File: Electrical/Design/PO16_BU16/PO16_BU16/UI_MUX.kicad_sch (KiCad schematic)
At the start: 18 parts, among them U1 74HC4051

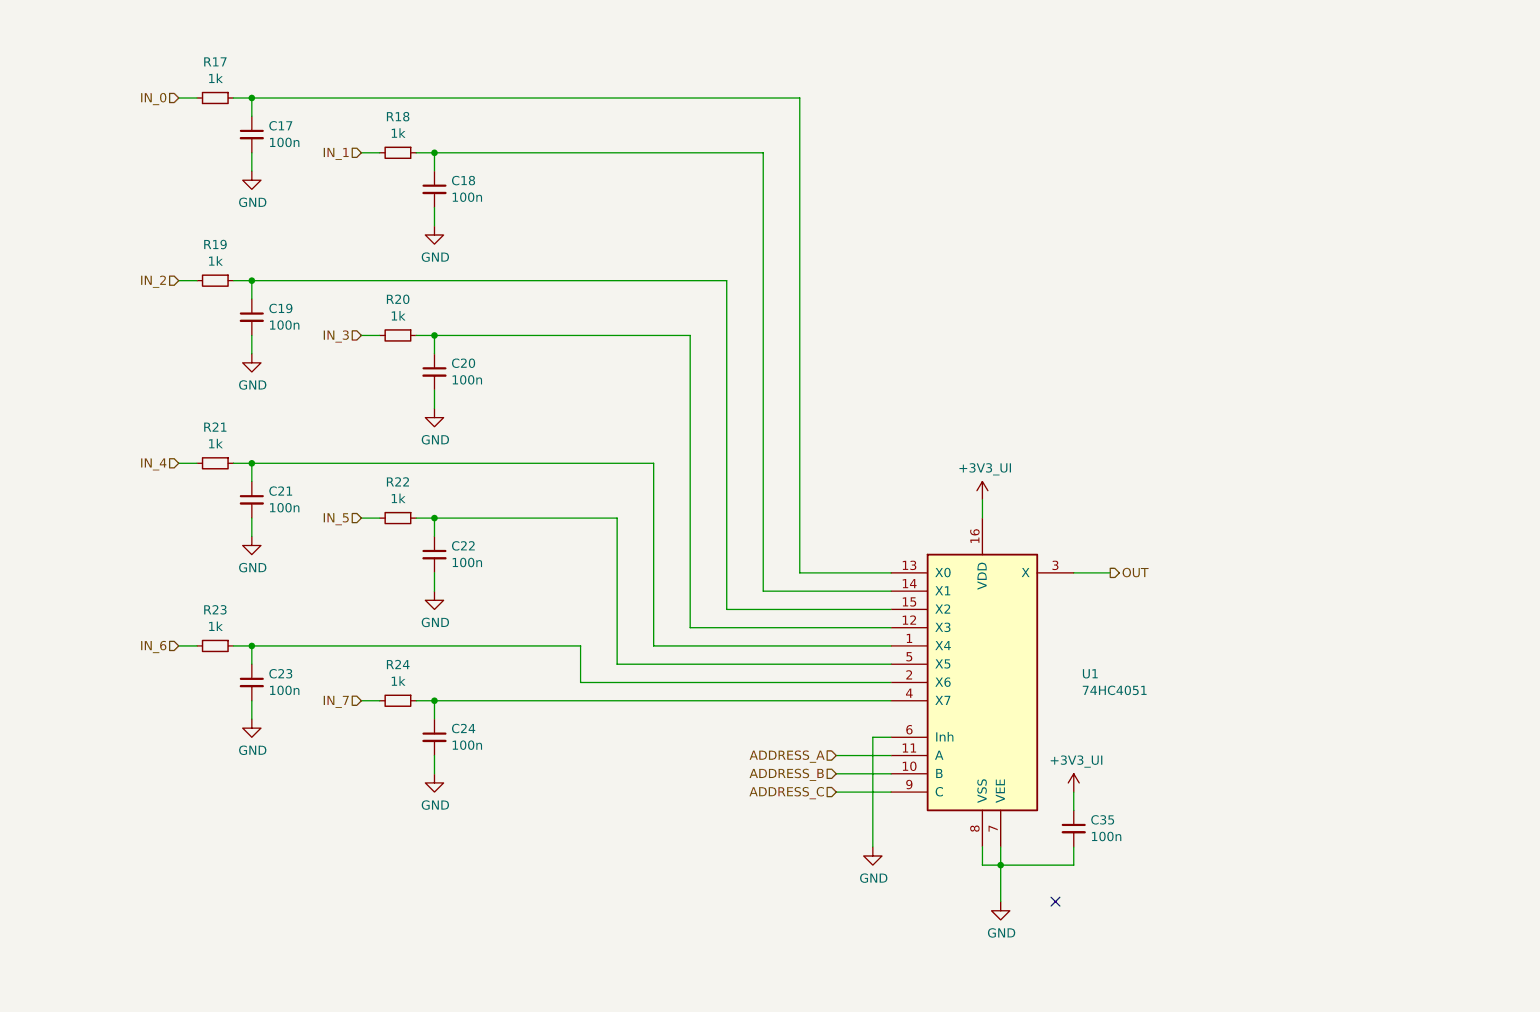
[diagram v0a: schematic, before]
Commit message: SUKU po16_bu16 cloned from pbf4
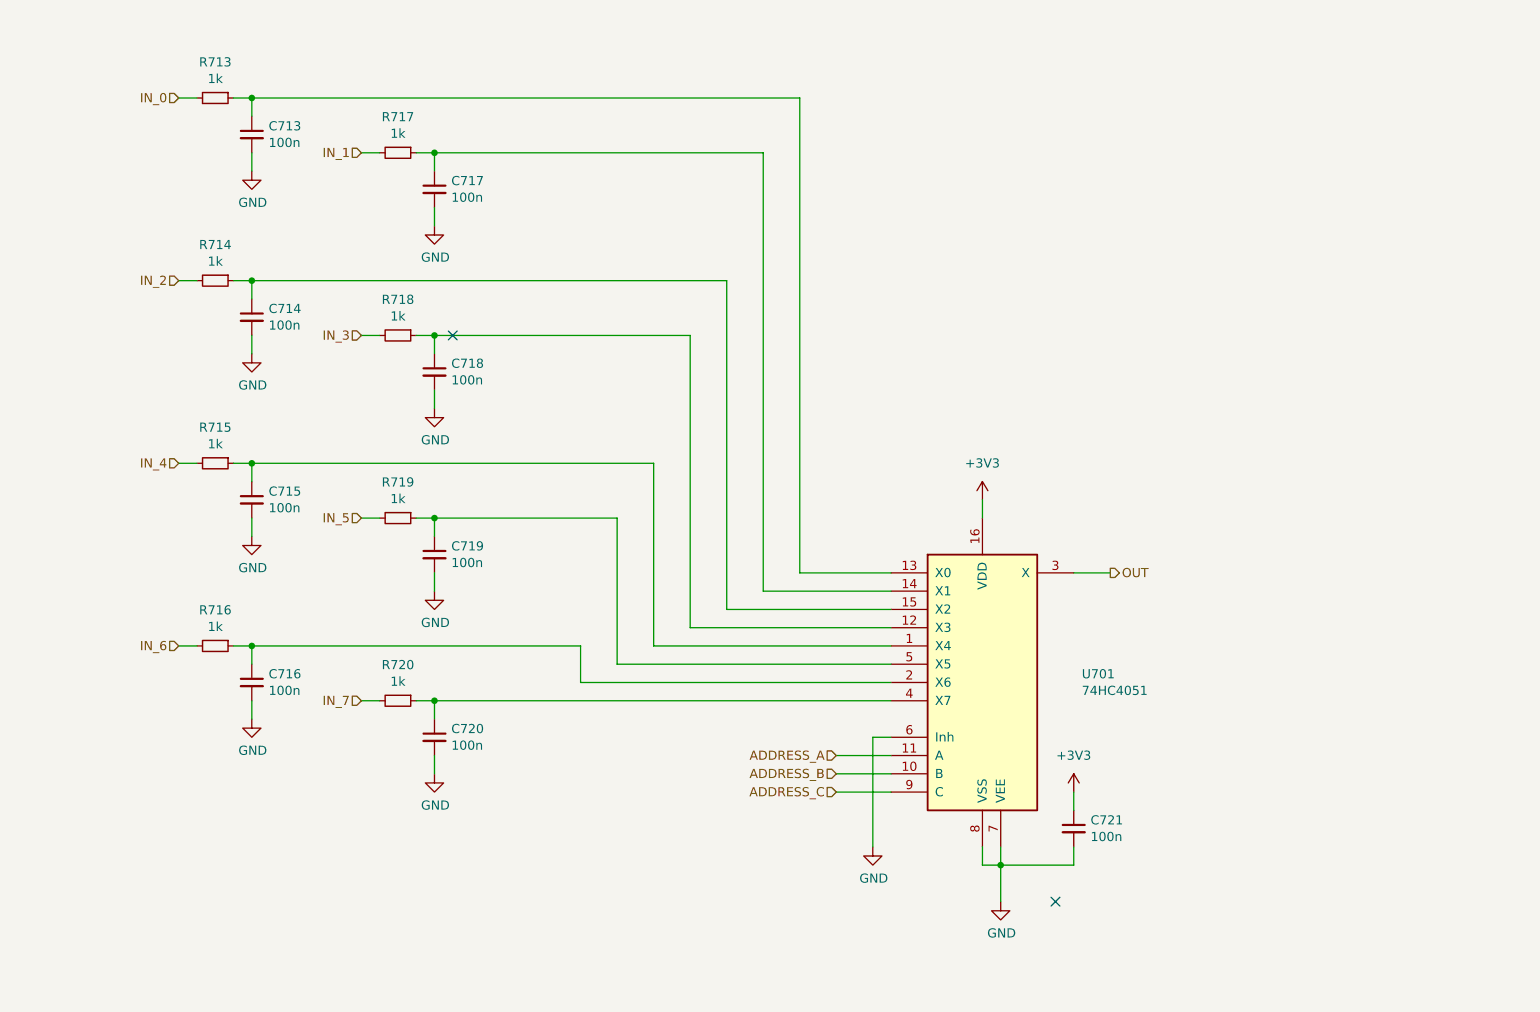
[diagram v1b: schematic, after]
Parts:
- C713: renamed from C17; footprint suku_basics:CAP_0805 -> suku_basics:CAP_0402
- C714: renamed from C19; footprint suku_basics:CAP_0805 -> suku_basics:CAP_0402
- C715: renamed from C21; footprint suku_basics:CAP_0805 -> suku_basics:CAP_0402
- C716: renamed from C23; footprint suku_basics:CAP_0805 -> suku_basics:CAP_0402
- C717: renamed from C18; footprint suku_basics:CAP_0805 -> suku_basics:CAP_0402
- C718: renamed from C20; footprint suku_basics:CAP_0805 -> suku_basics:CAP_0402
- C719: renamed from C22; footprint suku_basics:CAP_0805 -> suku_basics:CAP_0402
- C720: renamed from C24; footprint suku_basics:CAP_0805 -> suku_basics:CAP_0402
- C721: renamed from C35; footprint suku_basics:CAP_0805 -> suku_basics:CAP_0402
- R713: renamed from R17; footprint suku_basics:RES_0805 -> suku_basics:RES_0402
- R714: renamed from R19; footprint suku_basics:RES_0805 -> suku_basics:RES_0402
- R715: renamed from R21; footprint suku_basics:RES_0805 -> suku_basics:RES_0402
- R716: renamed from R23; footprint suku_basics:RES_0805 -> suku_basics:RES_0402
- R717: renamed from R18; footprint suku_basics:RES_0805 -> suku_basics:RES_0402
- R718: renamed from R20; footprint suku_basics:RES_0805 -> suku_basics:RES_0402
- R719: renamed from R22; footprint suku_basics:RES_0805 -> suku_basics:RES_0402
- R720: renamed from R24; footprint suku_basics:RES_0805 -> suku_basics:RES_0402
- renumbered U1 to U701
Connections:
- net +3V3_UI renamed +3V3
- no-connect marks 1 -> 2

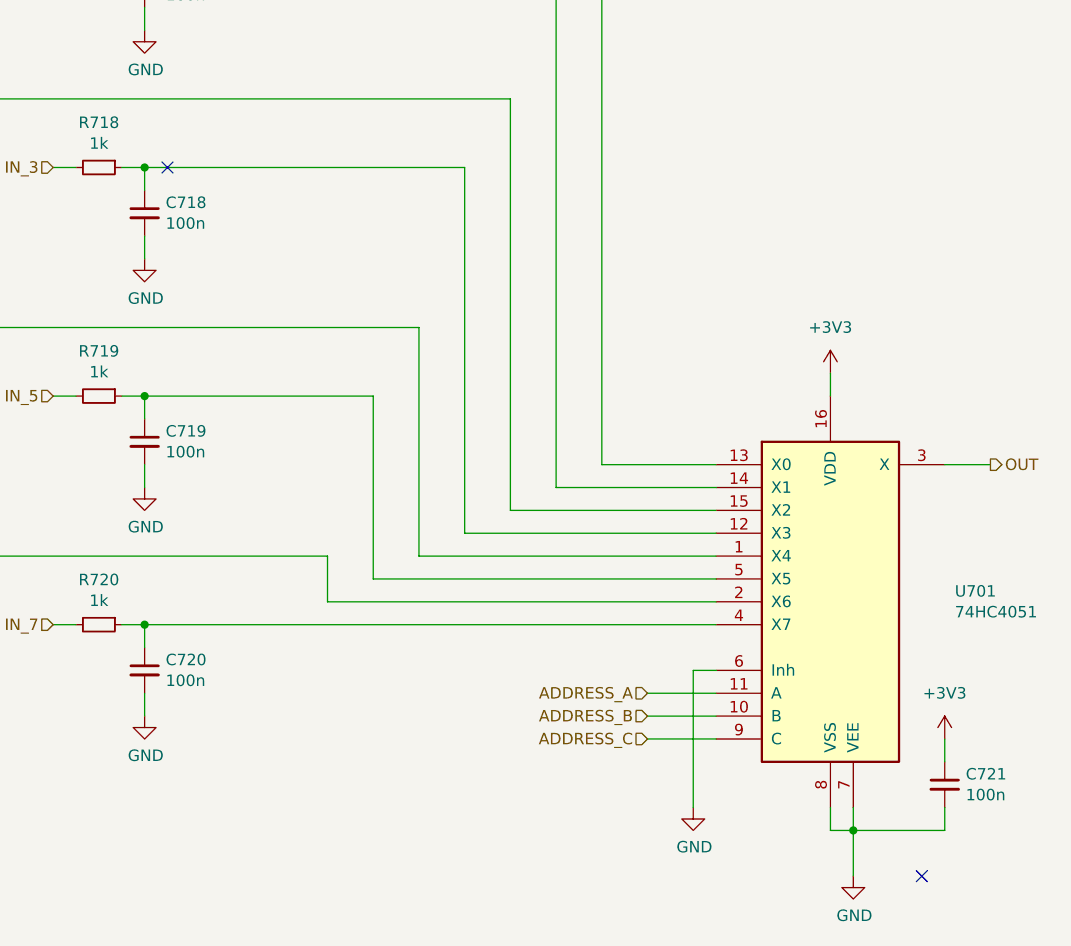
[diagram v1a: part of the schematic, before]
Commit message: SUKU PO16_BU16 updated design routed
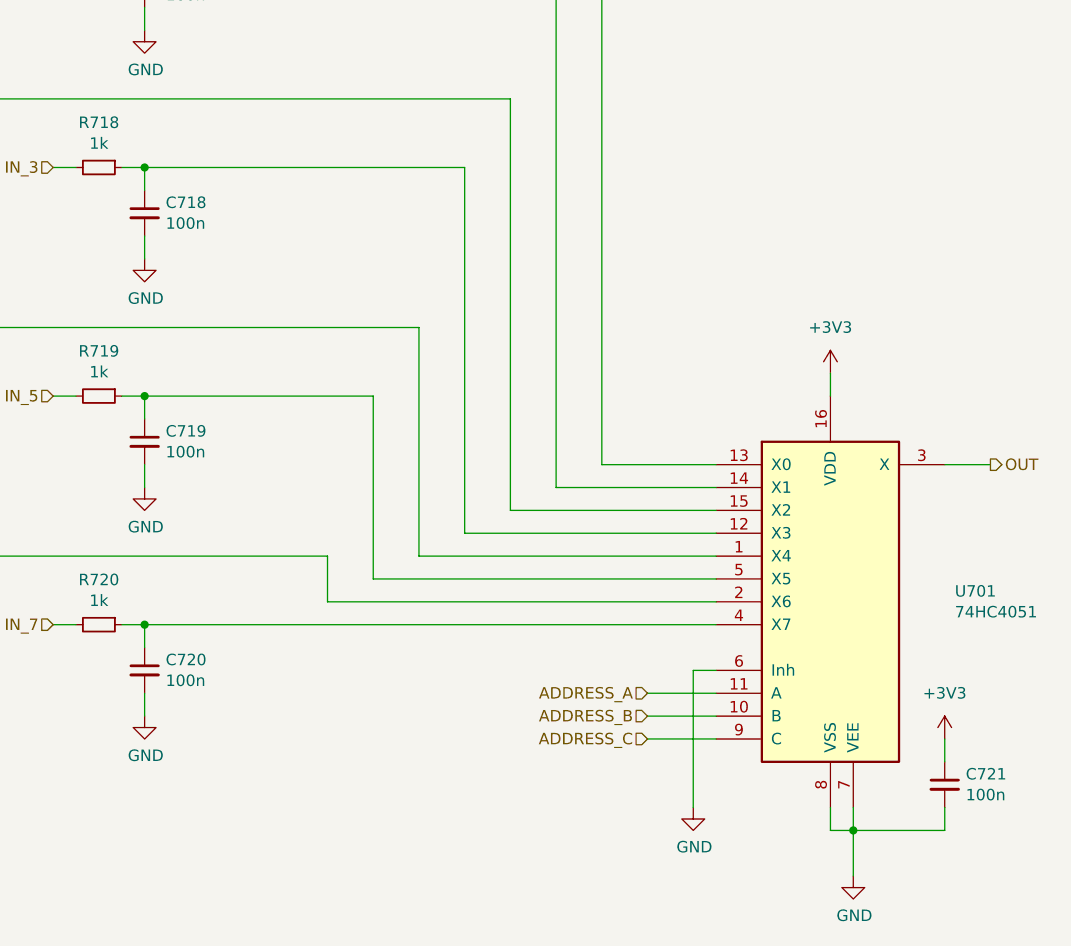
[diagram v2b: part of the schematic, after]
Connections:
- no-connect marks 2 -> 0
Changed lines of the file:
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@@
   (junction (at 154.94 132.08) (diameter 0) (color 0 0 0 0)
   )
-  (no_connect (at 162.56 137.16))
-  (no_connect (at 78.74 58.42))
   (wire (pts (xy 76.2 83.82) (xy 101.6 83.82))
     (stroke (width 0) (type default))
@@
     (pin "2")
     (instances
-      (project "PBF4"
+      (project "PO16_BU16"
         (path "/e5217a0c-7f55-4c30-adda-7f8d95709d1b/00000000-0000-0000-0000-00005d7c8bfe"
           (reference "C721") (unit 1)
@@
     (pin "1")
     (instances
-      (project "PBF4"
+      (project "PO16_BU16"
         (path "/e5217a0c-7f55-4c30-adda-7f8d95709d1b/00000000-0000-0000-0000-00005d7c8bfe"
           (reference "#PWR0779") (unit 1)
@@
     (pin "2")
     (instances
-      (project "PBF4"
+      (project "PO16_BU16"
         (path "/e5217a0c-7f55-4c30-adda-7f8d95709d1b/00000000-0000-0000-0000-00005d7c8bfe"
           (reference "R713") (unit 1)
@@
     (pin "2")
     (instances
-      (project "PBF4"
+      (project "PO16_BU16"
         (path "/e5217a0c-7f55-4c30-adda-7f8d95709d1b/00000000-0000-0000-0000-00005d7c8bfe"
           (reference "R717") (unit 1)
@@
     (pin "2")
     (instances
-      (project "PBF4"
+      (project "PO16_BU16"
         (path "/e5217a0c-7f55-4c30-adda-7f8d95709d1b/00000000-0000-0000-0000-00005d7c8bfe"
           (reference "R714") (unit 1)
@@
     (pin "2")
     (instances
-      (project "PBF4"
+      (project "PO16_BU16"
         (path "/e5217a0c-7f55-4c30-adda-7f8d95709d1b/00000000-0000-0000-0000-00005d7c8bfe"
           (reference "R718") (unit 1)
@@
     (pin "2")
     (instances
-      (project "PBF4"
+      (project "PO16_BU16"
         (path "/e5217a0c-7f55-4c30-adda-7f8d95709d1b/00000000-0000-0000-0000-00005d7c8bfe"
           (reference "R715") (unit 1)
@@
     (pin "2")
     (instances
-      (project "PBF4"
+      (project "PO16_BU16"
         (path "/e5217a0c-7f55-4c30-adda-7f8d95709d1b/00000000-0000-0000-0000-00005d7c8bfe"
           (reference "R719") (unit 1)
@@
     (pin "2")
     (instances
-      (project "PBF4"
+      (project "PO16_BU16"
         (path "/e5217a0c-7f55-4c30-adda-7f8d95709d1b/00000000-0000-0000-0000-00005d7c8bfe"
           (reference "R716") (unit 1)
@@
     (pin "2")
     (instances
-      (project "PBF4"
+      (project "PO16_BU16"
         (path "/e5217a0c-7f55-4c30-adda-7f8d95709d1b/00000000-0000-0000-0000-00005d7c8bfe"
           (reference "R720") (unit 1)
@@
     (pin "2")
     (instances
-      (project "PBF4"
+      (project "PO16_BU16"
         (path "/e5217a0c-7f55-4c30-adda-7f8d95709d1b/00000000-0000-0000-0000-00005d7c8bfe"
           (reference "C713") (unit 1)
@@
     (pin "1")
     (instances
-      (project "PBF4"
+      (project "PO16_BU16"
         (path "/e5217a0c-7f55-4c30-adda-7f8d95709d1b/00000000-0000-0000-0000-00005d7c8bfe"
           (reference "#PWR0769") (unit 1)
@@
     (pin "2")
     (instances
-      (project "PBF4"
+      (project "PO16_BU16"
         (path "/e5217a0c-7f55-4c30-adda-7f8d95709d1b/00000000-0000-0000-0000-00005d7c8bfe"
           (reference "C717") (unit 1)
@@
     (pin "1")
     (instances
-      (project "PBF4"
+      (project "PO16_BU16"
         (path "/e5217a0c-7f55-4c30-adda-7f8d95709d1b/00000000-0000-0000-0000-00005d7c8bfe"
           (reference "#PWR0773") (unit 1)
@@
     (pin "2")
     (instances
-      (project "PBF4"
+      (project "PO16_BU16"
         (path "/e5217a0c-7f55-4c30-adda-7f8d95709d1b/00000000-0000-0000-0000-00005d7c8bfe"
           (reference "C714") (unit 1)
@@
     (pin "1")
     (instances
-      (project "PBF4"
+      (project "PO16_BU16"
         (path "/e5217a0c-7f55-4c30-adda-7f8d95709d1b/00000000-0000-0000-0000-00005d7c8bfe"
           (reference "#PWR0770") (unit 1)
@@
     (pin "2")
     (instances
-      (project "PBF4"
+      (project "PO16_BU16"
         (path "/e5217a0c-7f55-4c30-adda-7f8d95709d1b/00000000-0000-0000-0000-00005d7c8bfe"
           (reference "C718") (unit 1)
@@
     (pin "1")
     (instances
-      (project "PBF4"
+      (project "PO16_BU16"
         (path "/e5217a0c-7f55-4c30-adda-7f8d95709d1b/00000000-0000-0000-0000-00005d7c8bfe"
           (reference "#PWR0774") (unit 1)
@@
     (pin "2")
     (instances
-      (project "PBF4"
+      (project "PO16_BU16"
         (path "/e5217a0c-7f55-4c30-adda-7f8d95709d1b/00000000-0000-0000-0000-00005d7c8bfe"
           (reference "C715") (unit 1)
@@
     (pin "1")
     (instances
-      (project "PBF4"
+      (project "PO16_BU16"
         (path "/e5217a0c-7f55-4c30-adda-7f8d95709d1b/00000000-0000-0000-0000-00005d7c8bfe"
           (reference "#PWR0771") (unit 1)
@@
     (pin "2")
     (instances
-      (project "PBF4"
+      (project "PO16_BU16"
         (path "/e5217a0c-7f55-4c30-adda-7f8d95709d1b/00000000-0000-0000-0000-00005d7c8bfe"
           (reference "C719") (unit 1)
@@
     (pin "1")
     (instances
-      (project "PBF4"
+      (project "PO16_BU16"
         (path "/e5217a0c-7f55-4c30-adda-7f8d95709d1b/00000000-0000-0000-0000-00005d7c8bfe"
           (reference "#PWR0775") (unit 1)
@@
     (pin "2")
     (instances
-      (project "PBF4"
+      (project "PO16_BU16"
         (path "/e5217a0c-7f55-4c30-adda-7f8d95709d1b/00000000-0000-0000-0000-00005d7c8bfe"
           (reference "C716") (unit 1)
@@
     (pin "1")
     (instances
-      (project "PBF4"
+      (project "PO16_BU16"
         (path "/e5217a0c-7f55-4c30-adda-7f8d95709d1b/00000000-0000-0000-0000-00005d7c8bfe"
           (reference "#PWR0772") (unit 1)
@@
     (pin "2")
     (instances
-      (project "PBF4"
+      (project "PO16_BU16"
         (path "/e5217a0c-7f55-4c30-adda-7f8d95709d1b/00000000-0000-0000-0000-00005d7c8bfe"
           (reference "C720") (unit 1)
@@
     (pin "1")
     (instances
-      (project "PBF4"
+      (project "PO16_BU16"
         (path "/e5217a0c-7f55-4c30-adda-7f8d95709d1b/00000000-0000-0000-0000-00005d7c8bfe"
           (reference "#PWR0776") (unit 1)
@@
     (pin "1")
     (instances
-      (project "PBF4"
+      (project "PO16_BU16"
         (path "/e5217a0c-7f55-4c30-adda-7f8d95709d1b/00000000-0000-0000-0000-00005d7c8bfe"
           (reference "#PWR0777") (unit 1)
@@
     (pin "9")
     (instances
-      (project "PBF4"
+      (project "PO16_BU16"
         (path "/e5217a0c-7f55-4c30-adda-7f8d95709d1b/00000000-0000-0000-0000-00005d7c8bfe"
           (reference "U701") (unit 1)
@@
     (pin "1")
     (instances
-      (project "PBF4"
+      (project "PO16_BU16"
         (path "/e5217a0c-7f55-4c30-adda-7f8d95709d1b/00000000-0000-0000-0000-00005d7c8bfe"
           (reference "#PWR0780") (unit 1)
@@
     (pin "1")
     (instances
-      (project "PBF4"
+      (project "PO16_BU16"
         (path "/e5217a0c-7f55-4c30-adda-7f8d95709d1b/00000000-0000-0000-0000-00005d7c8bfe"
           (reference "#PWR0778") (unit 1)
